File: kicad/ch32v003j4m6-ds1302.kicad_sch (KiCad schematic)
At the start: 11 parts, among them J1 Conn_01x04_Pin, SW1 SW_Push, U2 DS1302+, Y1 Crystal

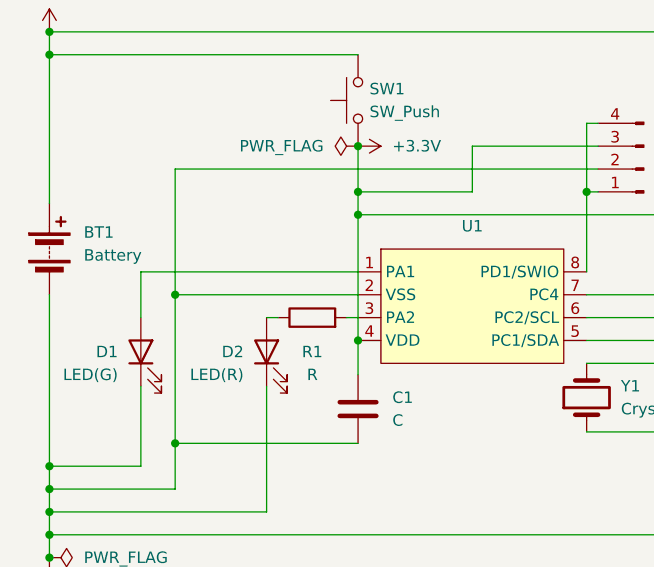
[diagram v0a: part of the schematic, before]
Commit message: Add a resistor for LED(G)
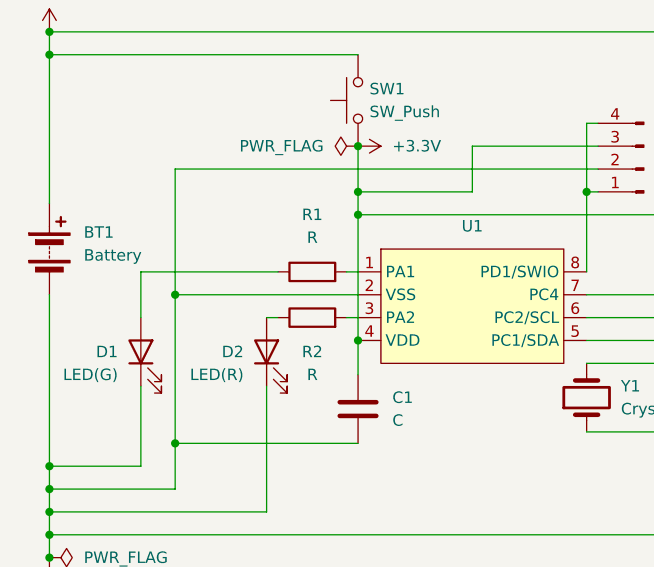
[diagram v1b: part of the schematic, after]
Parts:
- added R1: R, Resistor_SMD:R_0603_1608Metric, symbol Device:R
- renumbered R1 to R2
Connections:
- net at D1.2 (A): now also R1.1; no longer U1.1 (PA1)
- new net: R1.2, U1.1 (PA1)
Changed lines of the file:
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@@
+    (stroke (width 0) (type default))
+  )
+  (wire (pts (xy 69.85 55.88) (xy 71.12 55.88))
     (stroke (width 0) (type default))
   )
@@
     (stroke (width 0) (type default))
   )
-  (wire (pts (xy 46.99 55.88) (xy 71.12 55.88))
+  (wire (pts (xy 46.99 55.88) (xy 62.23 55.88))
     (stroke (width 0) (type default))
   )
@@
     (pin "1")
     (instances
-      (project "ch32v004jm6-ds1302"
+      (project "ch32v003j4m6-ds1302"
         (path "/f212f93a-e64a-4f8a-a74f-99b88de98049"
           (reference "#PWR08") (unit 1)
@@
     (pin "1")
     (instances
-      (project "ch32v004jm6-ds1302"
+      (project "ch32v003j4m6-ds1302"
         (path "/f212f93a-e64a-4f8a-a74f-99b88de98049"
           (reference "SW1") (unit 1)
@@
     (pin "2")
     (instances
-      (project "ch32v004jm6-ds1302"
+      (project "ch32v003j4m6-ds1302"
         (path "/f212f93a-e64a-4f8a-a74f-99b88de98049"
           (reference "Y1") (unit 1)
@@
   (symbol (lib_id "Device:R") (at 66.04 60.96 90) (unit 1)
     (in_bom yes) (on_board yes) (dnp no)
-    (property "Reference" "R1" (at 66.04 64.77 90)
+    (property "Reference" "R2" (at 66.04 64.77 90)
       (effects (font (size 1.27 1.27)))
     )
@@
     (pin "2")
     (instances
-      (project "ch32v004jm6-ds1302"
-        (path "/f212f93a-e64a-4f8a-a74f-99b88de98049"
-          (reference "R1") (unit 1)
+      (project "ch32v003j4m6-ds1302"
+        (path "/f212f93a-e64a-4f8a-a74f-99b88de98049"
+          (reference "R2") (unit 1)
         )
       )
@@
     (pin "2")
     (instances
-      (project "ch32v004jm6-ds1302"
+      (project "ch32v003j4m6-ds1302"
         (path "/f212f93a-e64a-4f8a-a74f-99b88de98049"
           (reference "D1") (unit 1)
@@
     (pin "2")
     (instances
-      (project "ch32v004jm6-ds1302"
+      (project "ch32v003j4m6-ds1302"
         (path "/f212f93a-e64a-4f8a-a74f-99b88de98049"
           (reference "U1") (unit 1)
@@
     (pin "2")
     (instances
-      (project "ch32v004jm6-ds1302"
+      (project "ch32v003j4m6-ds1302"
         (path "/f212f93a-e64a-4f8a-a74f-99b88de98049"
           (reference "BT1") (unit 1)
@@
     (pin "1")
     (instances
-      (project "ch32v004jm6-ds1302"
+      (project "ch32v003j4m6-ds1302"
         (path "/f212f93a-e64a-4f8a-a74f-99b88de98049"
           (reference "#FLG01") (unit 1)
@@
     (pin "4")
     (instances
-      (project "ch32v004jm6-ds1302"
+      (project "ch32v003j4m6-ds1302"
         (path "/f212f93a-e64a-4f8a-a74f-99b88de98049"
           (reference "J1") (unit 1)
@@
     (pin "2")
     (instances
-      (project "ch32v004jm6-ds1302"
+      (project "ch32v003j4m6-ds1302"
         (path "/f212f93a-e64a-4f8a-a74f-99b88de98049"
           (reference "U2") (unit 1)
@@
     (pin "2")
     (instances
-      (project "ch32v004jm6-ds1302"
+      (project "ch32v003j4m6-ds1302"
         (path "/f212f93a-e64a-4f8a-a74f-99b88de98049"
           (reference "D2") (unit 1)
@@
     (pin "1")
     (instances
-      (project "ch32v004jm6-ds1302"
+      (project "ch32v003j4m6-ds1302"
         (path "/f212f93a-e64a-4f8a-a74f-99b88de98049"
           (reference "#FLG03") (unit 1)
@@
     )
   )
+  (symbol (lib_id "Device:R") (at 66.04 55.88 90) (unit 1)
+    (in_bom yes) (on_board yes) (dnp no) (fields_autoplaced)
+    (property "Reference" "R1" (at 66.04 49.53 90)
+      (effects (font (size 1.27 1.27)))
+    )
+    (property "Value" "R" (at 66.04 52.07 90)
+      (effects (font (size 1.27 1.27)))
+    )
+    (property "Footprint" "Resistor_SMD:R_0603_1608Metric" (at 66.04 57.658 90)
+      (effects (font (size 1.27 1.27)) hide)
+    )
+    (property "Datasheet" "~" (at 66.04 55.88 0)
+      (effects (font (size 1.27 1.27)) hide)
+    )
+    (pin "2")
+    (pin "1")
+    (instances
+      (project "ch32v003j4m6-ds1302"
+        (path "/f212f93a-e64a-4f8a-a74f-99b88de98049"
+          (reference "R1") (unit 1)
+        )
+      )
+    )
+  )
   (symbol (lib_id "Device:C") (at 138.43 64.77 0) (unit 1)
     (in_bom yes) (on_board yes) (dnp no) (fields_autoplaced)
@@
     (pin "1")
     (instances
-      (project "ch32v004jm6-ds1302"
+      (project "ch32v003j4m6-ds1302"
         (path "/f212f93a-e64a-4f8a-a74f-99b88de98049"
           (reference "C2") (unit 1)
@@
     (pin "1")
     (instances
-      (project "ch32v004jm6-ds1302"
+      (project "ch32v003j4m6-ds1302"
         (path "/f212f93a-e64a-4f8a-a74f-99b88de98049"
           (reference "#FLG02") (unit 1)
@@
     (pin "1")
     (instances
-      (project "ch32v004jm6-ds1302"
+      (project "ch32v003j4m6-ds1302"
         (path "/f212f93a-e64a-4f8a-a74f-99b88de98049"
           (reference "C1") (unit 1)
@@
     (pin "1")
     (instances
-      (project "ch32v004jm6-ds1302"
+      (project "ch32v003j4m6-ds1302"
         (path "/f212f93a-e64a-4f8a-a74f-99b88de98049"
           (reference "#PWR09") (unit 1)
@@
     (pin "1")
     (instances
-      (project "ch32v004jm6-ds1302"
+      (project "ch32v003j4m6-ds1302"
         (path "/f212f93a-e64a-4f8a-a74f-99b88de98049"
           (reference "#PWR05") (unit 1)

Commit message: Fix mouting hole
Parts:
- added H1, H2, H3: MountingHole, MountingHole:MountingHole_3.2mm_M3, symbol Mechanical:MountingHole
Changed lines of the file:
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@@
+    )
+  )
+  (symbol (lib_id "Mechanical:MountingHole") (at 151.13 57.15 0) (unit 1)
+    (in_bom yes) (on_board yes) (dnp no) (fields_autoplaced)
+    (property "Reference" "H3" (at 153.67 55.88 0)
+      (effects (font (size 1.27 1.27)) (justify left))
+    )
+    (property "Value" "MountingHole" (at 153.67 58.42 0)
+      (effects (font (size 1.27 1.27)) (justify left))
+    )
+    (property "Footprint" "MountingHole:MountingHole_3.2mm_M3" (at 151.13 57.15 0)
+      (effects (font (size 1.27 1.27)) hide)
+    )
+    (property "Datasheet" "~" (at 151.13 57.15 0)
+      (effects (font (size 1.27 1.27)) hide)
+    )
+    (instances
+      (project "ch32v003j4m6-ds1302"
+        (path "/f212f93a-e64a-4f8a-a74f-99b88de98049"
+          (reference "H3") (unit 1)
+        )
+      )
     )
   )
@@
         (path "/f212f93a-e64a-4f8a-a74f-99b88de98049"
           (reference "C2") (unit 1)
+        )
+      )
+    )
+  )
+  (symbol (lib_id "Mechanical:MountingHole") (at 151.13 39.37 0) (unit 1)
+    (in_bom yes) (on_board yes) (dnp no) (fields_autoplaced)
+    (property "Reference" "H1" (at 153.67 38.1 0)
+      (effects (font (size 1.27 1.27)) (justify left))
+    )
+    (property "Value" "MountingHole" (at 153.67 40.64 0)
+      (effects (font (size 1.27 1.27)) (justify left))
+    )
+    (property "Footprint" "MountingHole:MountingHole_3.2mm_M3" (at 151.13 39.37 0)
+      (effects (font (size 1.27 1.27)) hide)
+    )
+    (property "Datasheet" "~" (at 151.13 39.37 0)
+      (effects (font (size 1.27 1.27)) hide)
+    )
+    (instances
+      (project "ch32v003j4m6-ds1302"
+        (path "/f212f93a-e64a-4f8a-a74f-99b88de98049"
+          (reference "H1") (unit 1)
         )
       )
@@
         )
       )
+    )
+  )
+  (symbol (lib_id "Mechanical:MountingHole") (at 151.13 48.26 0) (unit 1)
+    (in_bom yes) (on_board yes) (dnp no) (fields_autoplaced)
+    (property "Reference" "H2" (at 153.67 46.99 0)
+      (effects (font (size 1.27 1.27)) (justify left))
+    )
+    (property "Value" "MountingHole" (at 153.67 49.53 0)
+      (effects (font (size 1.27 1.27)) (justify left))
+    )
+    (property "Footprint" "MountingHole:MountingHole_3.2mm_M3" (at 151.13 48.26 0)
+      (effects (font (size 1.27 1.27)) hide)
+    )
+    (property "Datasheet" "~" (at 151.13 48.26 0)
+      (effects (font (size 1.27 1.27)) hide)
+    )
+    (instances
+      (project "ch32v003j4m6-ds1302"
+        (path "/f212f93a-e64a-4f8a-a74f-99b88de98049"
+          (reference "H2") (unit 1)
+        )
+      )

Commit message: Add title to sch
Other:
- company: (none) -> Tasuku Suzuki
- title: (none) -> Gathering CLOCK
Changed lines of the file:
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@@
 (kicad_sch (version 20230121) (generator eeschema)
   (paper "A4")
+  (title_block
+    (title "Gathering CLOCK")
+    (date "2024-02-05")
+    (rev "1.0")
+    (company "Tasuku Suzuki")
+  )
   (junction (at 71.12 41.91) (diameter 0) (color 0 0 0 0)
   )
